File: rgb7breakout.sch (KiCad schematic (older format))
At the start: 5 parts

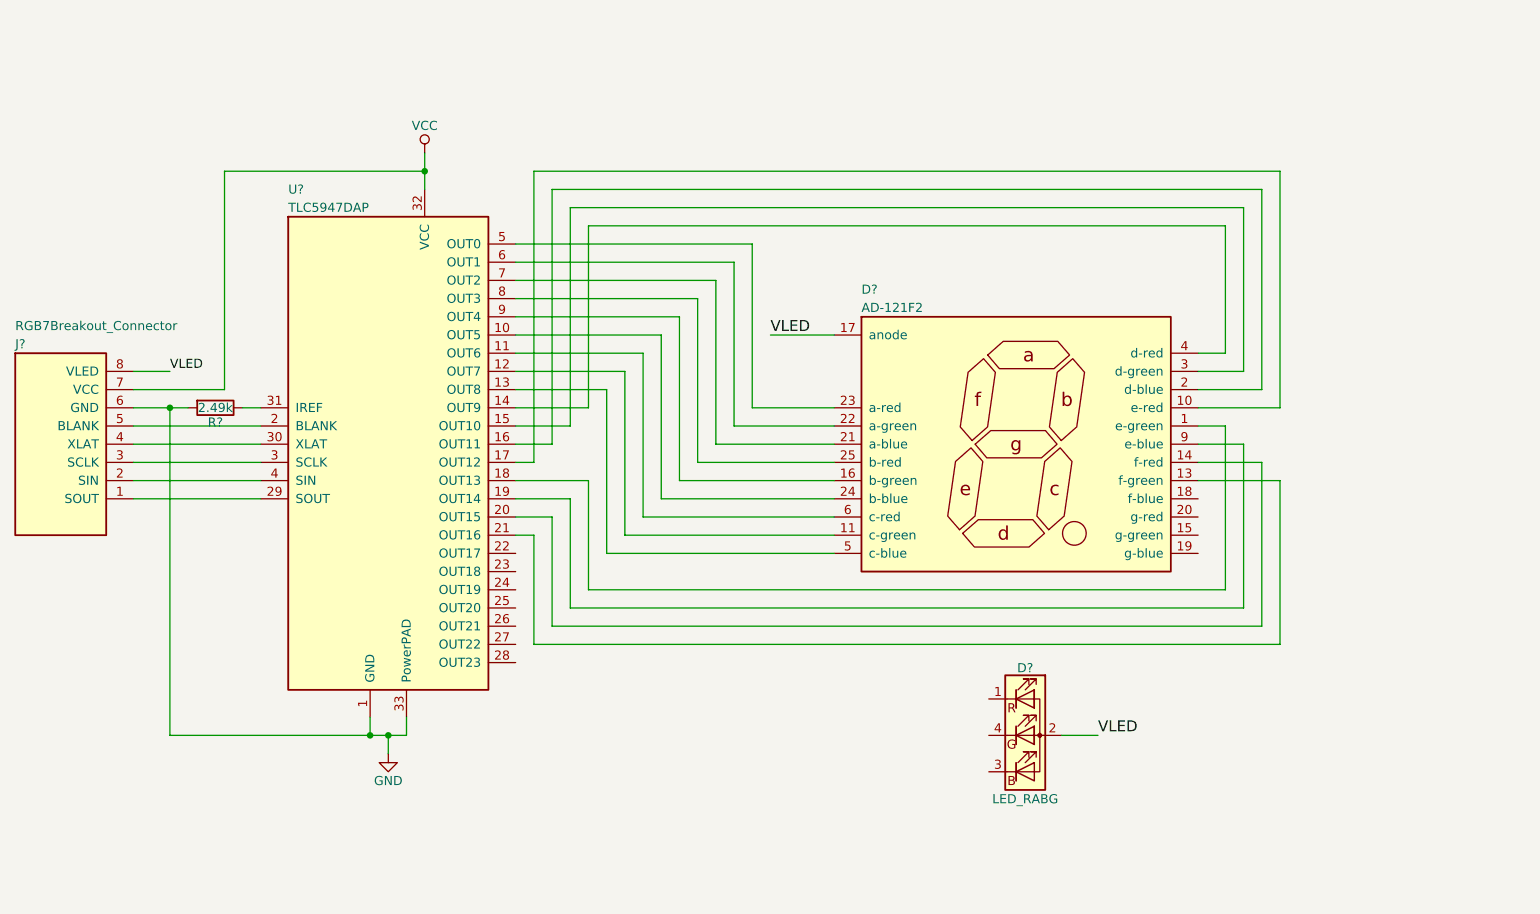
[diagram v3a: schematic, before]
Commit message: finish wires to LEDs
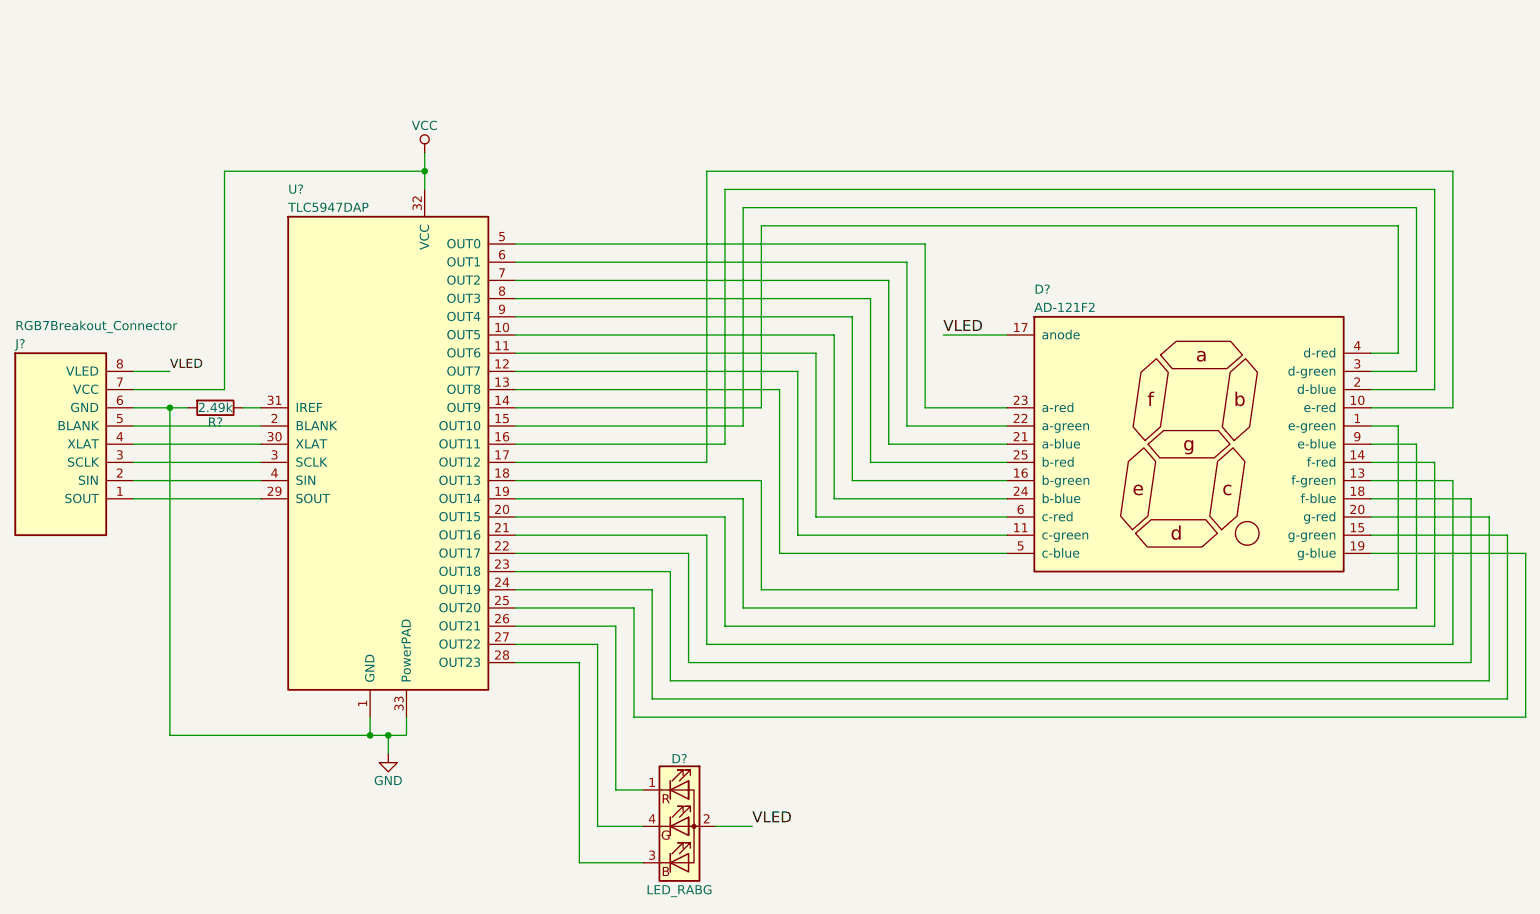
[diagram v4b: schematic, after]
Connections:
- net at D?.15 (g-green): now also U?.24 (OUT19)
- net at D?.18 (f-blue): now also U?.22 (OUT17)
- net at D?.19 (g-blue): now also U?.25 (OUT20)
- net at D?.20 (g-red): now also U?.23 (OUT18)
- net at U?.26 (OUT21): now also D?.1 (RK)
- net at U?.27 (OUT22): now also D?.4 (GK)
- net at U?.28 (OUT23): now also D?.3 (BK)
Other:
- moved on the sheet: D?
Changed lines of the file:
@@
 L AD-121F2 D?
 U 1 1 59B77441
-P 6950 3900
-F 0 "D?" H 6100 4750 50  0000 L CNN
-F 1 "AD-121F2" H 6100 4650 50  0000 L CNN
-F 2 "" H 6950 3900 50  0001 C CNN
-F 3 "" H 6950 3900 50  0001 C CNN
-	1    6950 3900
+P 7900 3900
+F 0 "D?" H 7050 4750 50  0000 L CNN
+F 1 "AD-121F2" H 7050 4650 50  0000 L CNN
+F 2 "" H 7900 3900 50  0001 C CNN
+F 3 "" H 7900 3900 50  0001 C CNN
+	1    7900 3900
 	1    0    0    -1
 $EndComp
@@
 L LED_RABG D?
 U 1 1 59B77822
-P 7000 5500
-F 0 "D?" H 7000 5870 50  0000 C CNN
-F 1 "LED_RABG" H 7000 5150 50  0000 C CNN
-F 2 "" H 7000 5450 50  0001 C CNN
-F 3 "" H 7000 5450 50  0001 C CNN
-F 4 "CLV1A-FKB-CHMKPEHBB7A363" H 7000 5500 60  0001 C CNN "ManufacturerPartNumber"
-F 5 "LED RGB DIFFUSED 4LCC SMD" H 7000 5500 60  0001 C CNN "Description"
-	1    7000 5500
+P 5100 6000
+F 0 "D?" H 5100 6370 50  0000 C CNN
+F 1 "LED_RABG" H 5100 5650 50  0000 C CNN
+F 2 "" H 5100 5950 50  0001 C CNN
+F 3 "" H 5100 5950 50  0001 C CNN
+F 4 "CLV1A-FKB-CHMKPEHBB7A363" H 5100 6000 60  0001 C CNN "ManufacturerPartNumber"
+F 5 "LED RGB DIFFUSED 4LCC SMD" H 5100 6000 60  0001 C CNN "Description"
+	1    5100 6000
 	1    0    0    -1
 $EndComp
@@
 	3500 5600 3500 5500
 Connection ~ 3500 5500
-Text Label 5600 3300 0    60   ~ 0
+Text Label 6550 3300 0    60   ~ 0
 VLED
-Text Label 7400 5500 0    60   ~ 0
+Text Label 5500 6000 0    60   ~ 0
 VLED
 Wire Wire Line
-	5600 3300 5950 3300
-Wire Wire Line
-	7200 5500 7400 5500
+	6550 3300 6900 3300
+Wire Wire Line
+	5300 6000 5500 6000
 $Comp
 L RGB7Breakout_Connector J?
@@
 Connection ~ 2300 3700
 Wire Wire Line
-	4200 2800 5500 2800
-Wire Wire Line
-	5500 2800 5500 3700
-Wire Wire Line
-	5500 3700 5950 3700
-Wire Wire Line
-	4200 2900 5400 2900
-Wire Wire Line
-	5400 2900 5400 3800
-Wire Wire Line
-	5400 3800 5950 3800
-Wire Wire Line
-	4200 3000 5300 3000
-Wire Wire Line
-	5300 3000 5300 3900
-Wire Wire Line
-	5300 3900 5950 3900
-Wire Wire Line
-	4200 3100 5200 3100
-Wire Wire Line
-	5200 3100 5200 4000
-Wire Wire Line
-	5200 4000 5950 4000
-Wire Wire Line
-	4200 3200 5100 3200
-Wire Wire Line
-	5100 3200 5100 4100
-Wire Wire Line
-	5100 4100 5950 4100
-Wire Wire Line
-	4200 3300 5000 3300
-Wire Wire Line
-	5000 3300 5000 4200
-Wire Wire Line
-	5000 4200 5950 4200
-Wire Wire Line
-	4200 3400 4900 3400
-Wire Wire Line
-	4900 3400 4900 4300
-Wire Wire Line
-	4900 4300 5950 4300
-Wire Wire Line
-	4200 3500 4800 3500
-Wire Wire Line
-	4800 3500 4800 4400
-Wire Wire Line
-	4800 4400 5950 4400
-Wire Wire Line
-	4200 3600 4700 3600
-Wire Wire Line
-	4700 3600 4700 4500
-Wire Wire Line
-	4700 4500 5950 4500
-Wire Wire Line
-	4200 3700 4600 3700
-Wire Wire Line
-	4600 3700 4600 2700
-Wire Wire Line
-	4600 2700 8100 2700
-Wire Wire Line
-	8100 2700 8100 3400
-Wire Wire Line
-	8100 3400 7950 3400
-Wire Wire Line
-	4200 3800 4500 3800
-Wire Wire Line
-	4500 3800 4500 2600
-Wire Wire Line
-	4500 2600 8200 2600
-Wire Wire Line
-	8200 2600 8200 3500
-Wire Wire Line
-	8200 3500 7950 3500
-Wire Wire Line
-	4200 3900 4400 3900
-Wire Wire Line
-	4400 3900 4400 2500
-Wire Wire Line
-	4400 2500 8300 2500
-Wire Wire Line
-	8300 2500 8300 3600
-Wire Wire Line
-	8300 3600 7950 3600
-Wire Wire Line
-	4200 4000 4300 4000
-Wire Wire Line
-	4300 4000 4300 2400
-Wire Wire Line
-	4300 2400 8400 2400
-Wire Wire Line
-	8400 2400 8400 3700
-Wire Wire Line
-	8400 3700 7950 3700
-Wire Wire Line
-	4200 4100 4600 4100
-Wire Wire Line
-	4600 4100 4600 4700
-Wire Wire Line
-	4600 4700 8100 4700
-Wire Wire Line
-	8100 4700 8100 3800
-Wire Wire Line
-	8100 3800 7950 3800
-Wire Wire Line
-	4200 4200 4500 4200
-Wire Wire Line
-	4500 4200 4500 4800
-Wire Wire Line
-	4500 4800 8200 4800
-Wire Wire Line
-	8200 4800 8200 3900
-Wire Wire Line
-	8200 3900 7950 3900
-Wire Wire Line
-	4200 4300 4400 4300
-Wire Wire Line
-	4400 4300 4400 4900
-Wire Wire Line
-	4400 4900 8300 4900
-Wire Wire Line
-	8300 4900 8300 4000
-Wire Wire Line
-	8300 4000 7950 4000
-Wire Wire Line
-	4200 4400 4300 4400
-Wire Wire Line
-	4300 4400 4300 5000
-Wire Wire Line
-	4300 5000 8400 5000
-Wire Wire Line
-	8400 5000 8400 4100
-Wire Wire Line
-	8400 4100 7950 4100
+	4200 2800 6450 2800
+Wire Wire Line
+	6450 2800 6450 3700
+Wire Wire Line
+	6450 3700 6900 3700
+Wire Wire Line
+	4200 2900 6350 2900
+Wire Wire Line
+	6350 2900 6350 3800
+Wire Wire Line
+	6350 3800 6900 3800
+Wire Wire Line
+	4200 3000 6250 3000
+Wire Wire Line
+	6250 3000 6250 3900
+Wire Wire Line
+	6250 3900 6900 3900
+Wire Wire Line
+	4200 3100 6150 3100
+Wire Wire Line
+	6150 3100 6150 4000
+Wire Wire Line
+	6150 4000 6900 4000
+Wire Wire Line
+	4200 3200 6050 3200
+Wire Wire Line
+	6050 3200 6050 4100
+Wire Wire Line
+	6050 4100 6900 4100
+Wire Wire Line
+	4200 3300 5950 3300
+Wire Wire Line
+	5950 3300 5950 4200
+Wire Wire Line
+	5950 4200 6900 4200
+Wire Wire Line
+	4200 3400 5850 3400
+Wire Wire Line
+	5850 3400 5850 4300
+Wire Wire Line
+	5850 4300 6900 4300
+Wire Wire Line
+	4200 3500 5750 3500
+Wire Wire Line
+	5750 3500 5750 4400
+Wire Wire Line
+	5750 4400 6900 4400
+Wire Wire Line
+	4200 3600 5650 3600
+Wire Wire Line
+	5650 3600 5650 4500
+Wire Wire Line
+	5650 4500 6900 4500
+Wire Wire Line
+	4200 3700 5550 3700
+Wire Wire Line
+	5550 3700 5550 2700
+Wire Wire Line
+	5550 2700 9050 2700
+Wire Wire Line
+	9050 2700 9050 3400
+Wire Wire Line
+	9050 3400 8900 3400
+Wire Wire Line
+	4200 3800 5450 3800
+Wire Wire Line
+	5450 3800 5450 2600
+Wire Wire Line
+	5450 2600 9150 2600
+Wire Wire Line
+	9150 2600 9150 3500
+Wire Wire Line
+	9150 3500 8900 3500
+Wire Wire Line
+	4200 3900 5350 3900
+Wire Wire Line
+	5350 3900 5350 2500
+Wire Wire Line
+	5350 2500 9250 2500
+Wire Wire Line
+	9250 2500 9250 3600
+Wire Wire Line
+	9250 3600 8900 3600
+Wire Wire Line
+	4200 4000 5250 4000
+Wire Wire Line
+	5250 4000 5250 2400
+Wire Wire Line
+	5250 2400 9350 2400
+Wire Wire Line
+	9350 2400 9350 3700
+Wire Wire Line
+	9350 3700 8900 3700
+Wire Wire Line
+	4200 4100 5550 4100
+Wire Wire Line
+	5550 4100 5550 4700
+Wire Wire Line
+	5550 4700 9050 4700
+Wire Wire Line
+	9050 4700 9050 3800
+Wire Wire Line
+	9050 3800 8900 3800
+Wire Wire Line
+	4200 4200 5450 4200
+Wire Wire Line
+	5450 4200 5450 4800
+Wire Wire Line
+	5450 4800 9150 4800
+Wire Wire Line
+	9150 4800 9150 3900
+Wire Wire Line
+	9150 3900 8900 3900
+Wire Wire Line
+	4200 4300 5350 4300
+Wire Wire Line
+	5350 4300 5350 4900
+Wire Wire Line
+	5350 4900 9250 4900
+Wire Wire Line
+	9250 4900 9250 4000
+Wire Wire Line
+	9250 4000 8900 4000
+Wire Wire Line
+	4200 4400 5250 4400
+Wire Wire Line
+	5250 4400 5250 5000
+Wire Wire Line
+	5250 5000 9350 5000
+Wire Wire Line
+	9350 5000 9350 4100
+Wire Wire Line
+	9350 4100 8900 4100
+Wire Wire Line
+	4200 4500 5150 4500
+Wire Wire Line
+	5150 4500 5150 5100
+Wire Wire Line
+	5150 5100 9450 5100
+Wire Wire Line
+	9450 5100 9450 4200
+Wire Wire Line
+	9450 4200 8900 4200
+Wire Wire Line
+	4200 4600 5050 4600
+Wire Wire Line
+	5050 4600 5050 5200
+Wire Wire Line
+	5050 5200 9550 5200
+Wire Wire Line
+	9550 5200 9550 4300
+Wire Wire Line
+	9550 4300 8900 4300
+Wire Wire Line
+	4200 4700 4950 4700
+Wire Wire Line
+	4950 4700 4950 5300
+Wire Wire Line
+	4950 5300 9650 5300
+Wire Wire Line
+	9650 5300 9650 4400
+Wire Wire Line
+	9650 4400 8900 4400
+Wire Wire Line
+	4200 4800 4850 4800
+Wire Wire Line
+	4850 4800 4850 5400
+Wire Wire Line
+	4850 5400 9750 5400
+Wire Wire Line
+	9750 5400 9750 4500
+Wire Wire Line
+	9750 4500 8900 4500
+Wire Wire Line
+	4200 4900 4750 4900
+Wire Wire Line
+	4750 4900 4750 5800
+Wire Wire Line
+	4750 5800 4900 5800
+Wire Wire Line
+	4200 5000 4650 5000
+Wire Wire Line
+	4650 5000 4650 6000
+Wire Wire Line
+	4650 6000 4900 6000
+Wire Wire Line
+	4200 5100 4550 5100
+Wire Wire Line
+	4550 5100 4550 6200
+Wire Wire Line
+	4550 6200 4900 6200
 $EndSCHEMATC

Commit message: added some decoupling capacitors
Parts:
- added C?: 100uF, symbol CP1
- added C?: 0.1uF, symbol C
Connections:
- net GND: now also C?.2, C?.2
- net VCC: now also C?.1
- net VLED: now also C?.1
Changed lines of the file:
@@
 	3500 5600 3500 5500
 Connection ~ 3500 5500
-Text Label 6550 3300 0    60   ~ 0
+Text Label 6100 1650 0    60   ~ 0
 VLED
 Text Label 5500 6000 0    60   ~ 0
 VLED
-Wire Wire Line
-	6550 3300 6900 3300
 Wire Wire Line
 	5300 6000 5500 6000
@@
 Wire Wire Line
 	4550 6200 4900 6200
+$Comp
+L CP1 C?
+U 1 1 59B79947
+P 6400 1900
+F 0 "C?" H 6425 2000 50  0000 L CNN
+F 1 "100uF" H 6425 1800 50  0000 L CNN
+F 2 "" H 6400 1900 50  0001 C CNN
+F 3 "" H 6400 1900 50  0001 C CNN
+F 4 "107SML016M" H 6400 1900 60  0001 C CNN "ManufacturerPartNumber"
+F 5 "CAP ALUM 100UF 20% 16V SMD" H 6400 1900 60  0001 C CNN "Description"
+	1    6400 1900
+	1    0    0    -1
+$EndComp
+$Comp
+L VCC #PWR?
+U 1 1 59B799AD
+P 2700 4900
+F 0 "#PWR?" H 2700 4750 50  0001 C CNN
+F 1 "VCC" H 2700 5050 50  0000 C CNN
+F 2 "" H 2700 4900 50  0001 C CNN
+F 3 "" H 2700 4900 50  0001 C CNN
+	1    2700 4900
+	1    0    0    -1
+$EndComp
+Wire Wire Line
+	2700 4900 2700 5000
+Wire Wire Line
+	2700 5300 2700 5500
+Connection ~ 2700 5500
+$Comp
+L C C?
+U 1 1 59B79BCD
+P 2700 5150
+F 0 "C?" H 2725 5250 50  0000 L CNN
+F 1 "0.1uF" H 2725 5050 50  0000 L CNN
+F 2 "" H 2738 5000 50  0001 C CNN
+F 3 "" H 2700 5150 50  0001 C CNN
+	1    2700 5150
+	1    0    0    -1
+$EndComp
+Wire Wire Line
+	6900 3300 6800 3300
+Wire Wire Line
+	6800 3300 6800 1650
+Wire Wire Line
+	6800 1650 6100 1650
+Wire Wire Line
+	6400 1750 6400 1650
+Connection ~ 6400 1650
+$Comp
+L GND #PWR?
+U 1 1 59B79DA4
+P 6400 2150
+F 0 "#PWR?" H 6400 1900 50  0001 C CNN
+F 1 "GND" H 6400 2000 50  0000 C CNN
+F 2 "" H 6400 2150 50  0001 C CNN
+F 3 "" H 6400 2150 50  0001 C CNN
+	1    6400 2150
+	1    0    0    -1
+$EndComp
+Wire Wire Line
+	6400 2050 6400 2150
 $EndSCHEMATC

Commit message: use house parts for capacitors
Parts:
- C?: Description CAP ALUM 100UF 20% 16V SMD -> Capacitor Aluminum Electrolytic 6.3mm 100uF 20% 35V; ManufacturerPartNumber 107SML016M -> MF-CAP-6.3MM-100uF
- C?: Description (none) -> Capacitor MLCC 0603 0.1uF 10% 25V; ManufacturerPartNumber (none) -> MF-CAP-0603-0.1uF
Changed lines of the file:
@@
 F 2 "" H 6400 1900 50  0001 C CNN
 F 3 "" H 6400 1900 50  0001 C CNN
-F 4 "107SML016M" H 6400 1900 60  0001 C CNN "ManufacturerPartNumber"
-F 5 "CAP ALUM 100UF 20% 16V SMD" H 6400 1900 60  0001 C CNN "Description"
+F 4 "MF-CAP-6.3MM-100uF" H 6400 1900 60  0001 C CNN "ManufacturerPartNumber"
+F 5 "Capacitor Aluminum Electrolytic 6.3mm 100uF 20% 35V" H 6400 1900 60  0001 C CNN "Description"
 	1    6400 1900
 	1    0    0    -1
@@
 F 2 "" H 2738 5000 50  0001 C CNN
 F 3 "" H 2700 5150 50  0001 C CNN
+F 4 "MF-CAP-0603-0.1uF" H 2700 5150 60  0001 C CNN "ManufacturerPartNumber"
+F 5 "Capacitor MLCC 0603 0.1uF 10% 25V" H 2700 5150 60  0001 C CNN "Description"
 	1    2700 5150
 	1    0    0    -1

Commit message: pulldown resistor for BLANK
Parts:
- added R?: 10k, symbol R
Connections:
- net GND: now also R?.2
- net at J?.5 (BLANK), U?.2 (BLANK): now also R?.1
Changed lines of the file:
@@
 Wire Wire Line
 	6400 2050 6400 2150
+$Comp
+L R R?
+U 1 1 59B7A418
+P 2450 4450
+F 0 "R?" V 2530 4450 50  0000 C CNN
+F 1 "10k" V 2450 4450 50  0000 C CNN
+F 2 "" V 2380 4450 50  0001 C CNN
+F 3 "" H 2450 4450 50  0001 C CNN
+F 4 "MF-RES-0603-10K" H 2450 4450 60  0001 C CNN "ManufacturerPartNumber"
+F 5 "Resistor Thick Film 0603 10K Ohm 5% 100mW 75V" H 2450 4450 60  0001 C CNN "Description"
+	1    2450 4450
+	1    0    0    -1
+$EndComp
+Wire Wire Line
+	2450 4300 2450 3800
+Connection ~ 2450 3800
+Wire Wire Line
+	2450 4600 2450 4700
+Wire Wire Line
+	2450 4700 2300 4700
+Connection ~ 2300 4700
 $EndSCHEMATC

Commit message: use QFN package instead of HTSSOP
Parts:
- removed U?: TLC5947DAP, symbol TLC5947DAP
- added U?: TLC5947RHB, symbol TLC5947RHB
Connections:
- net GND: now also U?.29 (GND), U?.33 (PowerPAD)
- net VCC: now also U?.28 (VCC)
- net at D?.1 (e-green): now also U?.14 (OUT13)
- net at D?.10 (e-red): now also U?.13 (OUT12)
- net at D?.11 (c-green): now also U?.8 (OUT7)
- net at D?.13 (f-green): now also U?.17 (OUT16)
- net at D?.14 (f-red): now also U?.16 (OUT15)
- net at D?.15 (g-green): now also U?.20 (OUT19)
- net at D?.16 (b-green): now also U?.5 (OUT4)
- net at D?.18 (f-blue): now also U?.18 (OUT17)
- net at D?.19 (g-blue): now also U?.21 (OUT20)
- net at D?.2 (d-blue): now also U?.12 (OUT11)
- net at D?.20 (g-red): now also U?.19 (OUT18)
- net at D?.21 (a-blue): now also U?.3 (OUT2)
- net at D?.22 (a-green): now also U?.2 (OUT1)
- net at D?.23 (a-red): now also U?.1 (OUT0)
- net at D?.24 (b-blue): now also U?.6 (OUT5)
- net at D?.25 (b-red): now also U?.4 (OUT3)
- net at D?.3 (d-green): now also U?.11 (OUT10)
- net at D?.4 (d-red): now also U?.10 (OUT9)
- net at D?.5 (c-blue): now also U?.9 (OUT8)
- net at D?.6 (c-red): now also U?.7 (OUT6)
- net at D?.9 (e-blue): now also U?.15 (OUT14)
- net at J?.5 (BLANK), R?.1: now also U?.30 (BLANK)
- net at D?.1 (RK): now also U?.22 (OUT21)
- net at D?.4 (GK): now also U?.23 (OUT22)
- net at D?.3 (BK): now also U?.24 (OUT23)
- net at J?.1 (SOUT): now also U?.25 (SOUT)
- net at J?.3 (SCLK): now also U?.31 (SCLK)
- net at J?.4 (XLAT): now also U?.26 (XLAT)
- net at R?.1: now also U?.27 (IREF)
- net at J?.2 (SIN): now also U?.32 (SIN)
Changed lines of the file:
@@
-$EndComp
-$Comp
-L TLC5947DAP U?
-U 1 1 59B77464
-P 3500 4000
-F 0 "U?" H 2950 5500 50  0000 L CNN
-F 1 "TLC5947DAP" H 2950 5400 50  0000 L CNN
-F 2 "" H 3500 4000 50  0001 C CNN
-F 3 "" H 3500 4000 50  0001 C CNN
-	1    3500 4000
-	1    0    0    -1
 $EndComp
 $Comp
@@
 	2450 4700 2300 4700
 Connection ~ 2300 4700
+$Comp
+L TLC5947RHB U?
+U 1 1 59B82404
+P 3500 4000
+F 0 "U?" H 2950 5500 50  0000 L CNN
+F 1 "TLC5947RHB" H 2950 5400 50  0000 L CNN
+F 2 "" H 3500 4000 50  0001 C CNN
+F 3 "" H 3500 4000 50  0001 C CNN
+	1    3500 4000
+	1    0    0    -1
+$EndComp
 $EndSCHEMATC
